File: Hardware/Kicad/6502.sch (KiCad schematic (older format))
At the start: 4 parts, among them IC401 65[C]02, K401 SYNC DEBUG CLK2

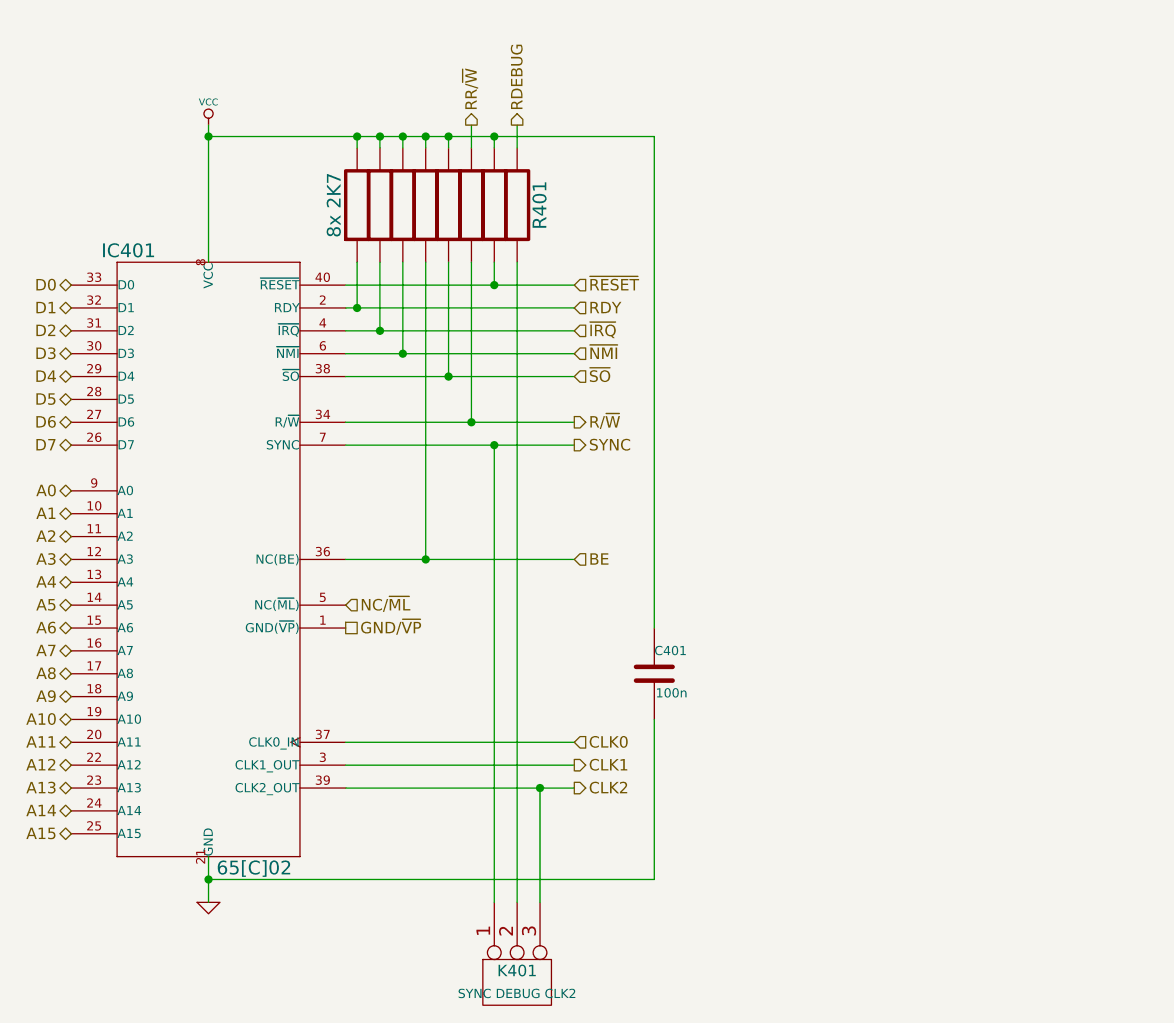
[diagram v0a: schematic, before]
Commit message: Schematic updates
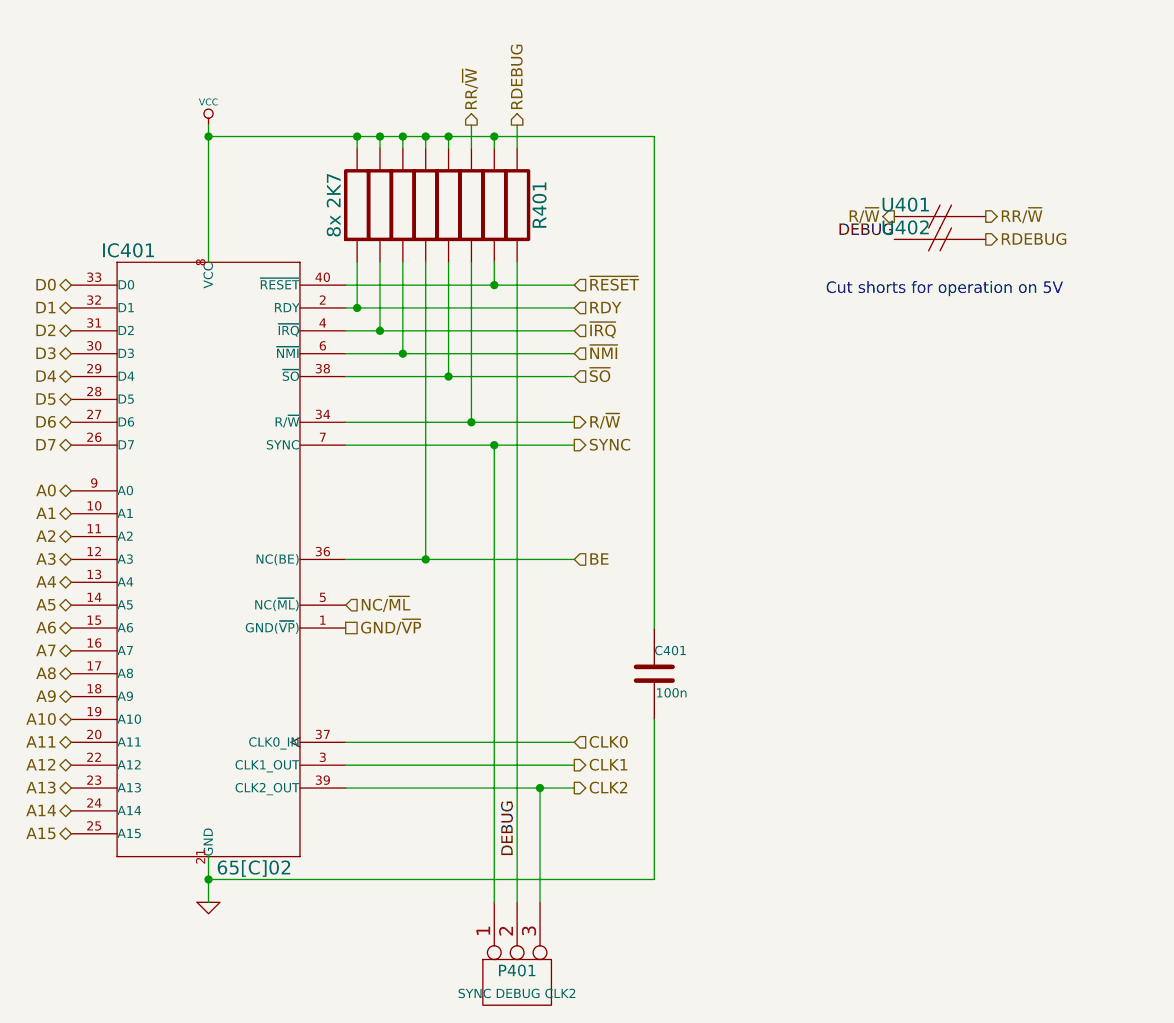
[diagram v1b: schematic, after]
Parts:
- added U401, U402: ~, symbol 00JG-SHORT
- renumbered K401 to P401
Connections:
- net R/~W: now also U401.1
- net RDEBUG: now also U402.2
- net RR/~W: now also U401.2
- net DEBUG: now reaches P401.2 (PM), R401.8
- net DEBUG: now also U402.1
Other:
- note added: "Cut shorts for operation on 5V"
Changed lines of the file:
@@
 Sheet 4 7
 Title "Propeddle"
-Date "8 apr 2014"
+Date "18 apr 2014"
 Rev "10"
 Comp "(C) 2014 Jac Goudsmit"
@@
 RDEBUG
 $Comp
-L CONN_3 K401
+L CONN_3 P401
 U 1 1 53483773
 P 6300 6250
-F 0 "K401" V 6250 6250 50  0000 C CNN
+F 0 "P401" V 6250 6250 50  0000 C CNN
 F 1 "SYNC DEBUG CLK2" V 6350 6250 40  0000 C CNN
 F 2 "~" H 6300 6250 60  0000 C CNN
@@
 	6400 5900 6400 5400
 Connection ~ 6400 5400
+$Comp
+L 00JG-SHORT U401
+U 1 1 534C5202
+P 8150 2900
+F 0 "U401" H 8000 2950 60  0000 C CNN
+F 1 "~" H 8150 2700 60  0000 C CNN
+F 2 "" H 8150 2900 60  0000 C CNN
+F 3 "" H 8150 2900 60  0000 C CNN
+	1    8150 2900
+	1    0    0    -1
+$EndComp
+$Comp
+L 00JG-SHORT U402
+U 1 1 534C520F
+P 8150 3000
+F 0 "U402" H 8000 3050 60  0000 C CNN
+F 1 "~" H 8150 2800 60  0000 C CNN
+F 2 "" H 8150 3000 60  0000 C CNN
+F 3 "" H 8150 3000 60  0000 C CNN
+	1    8150 3000
+	1    0    0    -1
+$EndComp
+Text HLabel 8350 2900 2    50   Output ~ 0
+RR/~W
+Text HLabel 8350 3000 2    50   Output ~ 0
+RDEBUG
+Text HLabel 7950 2900 0    50   Output ~ 0
+R/~W
+Text Notes 7650 3250 0    50   ~ 0
+Cut shorts for operation on 5V
+Text Label 6300 5700 1    50   ~ 0
+DEBUG
+Text Label 7950 3000 2    50   ~ 0
+DEBUG
 $EndSCHEMATC
